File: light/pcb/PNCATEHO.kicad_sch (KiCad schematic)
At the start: 49 parts, among them J1 USB_C_Receptacle_USB2.0, U1 RP2040, U2 RT9013-33GB, U3 W25Q32JVSSIQ, Y1 12MHz

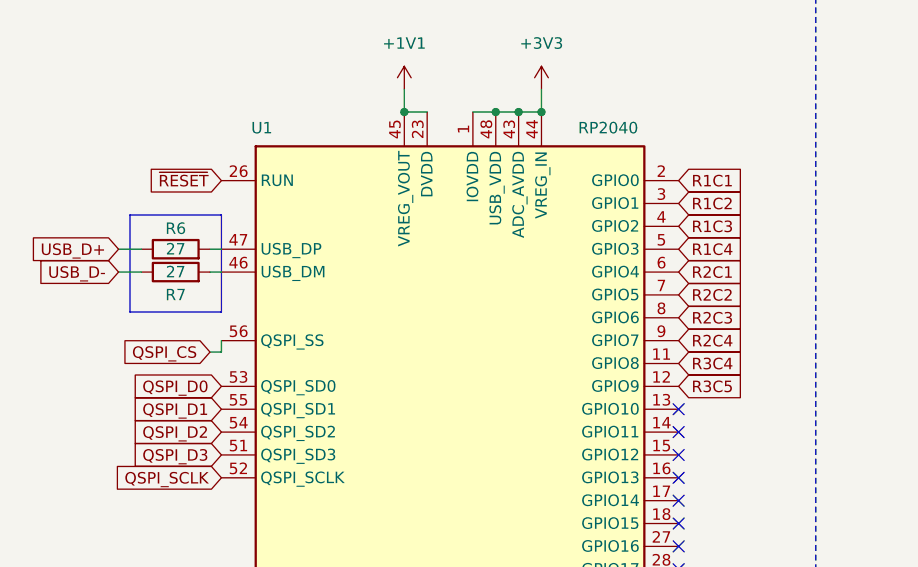
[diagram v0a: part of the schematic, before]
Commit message: PGS1316s PNCATEHO basic routing
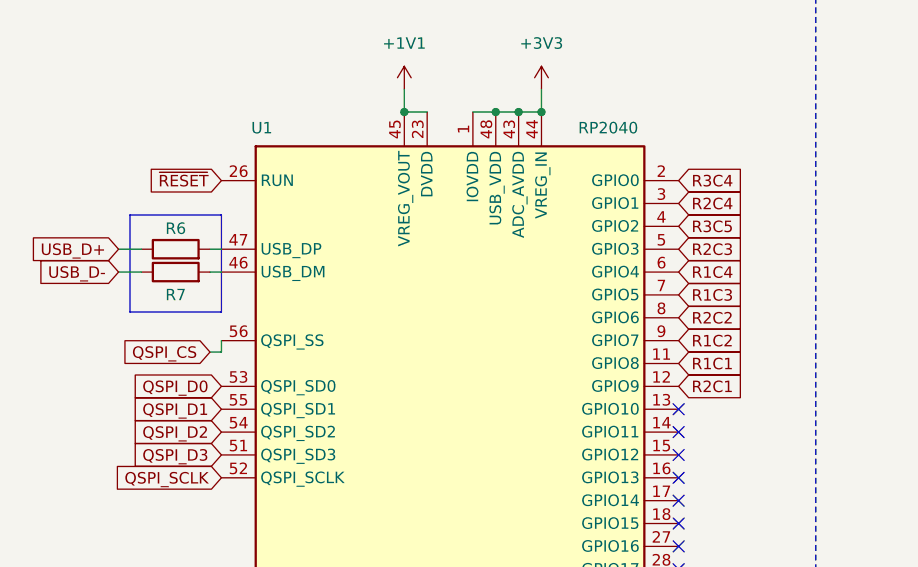
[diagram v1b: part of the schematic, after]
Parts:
- C1, C10, C11, C12, C13, C14, C15, C16, C2, C3, C4, C5, C6, C7, C8, C9: footprint footprint:C_0805_2012Metric_Pad1.18x1.45mm_HandSolder -> PNCATEHO:C_0805_2012Metric_Pad1.18x1.45mm_HandSolder
- D1, D2: footprint footprint:LED_0805_2012Metric_Pad1.15x1.40mm_HandSolder -> PNCATEHO:LED_0805_2012Metric_Pad1.15x1.40mm_HandSolder
- F1: footprint footprint:Fuse_0805_2012Metric -> PNCATEHO:Fuse_0805_2012Metric
- J1: footprint footprint:USB_C_Receptacle_TYPE-C-31-M-12 -> PNCATEHO:USB_C_Receptacle_TYPE-C-31-M-12
- R1, R10, R2, R3, R4, R5, R6, R7, R8, R9: footprint footprint:R_0805_2012Metric_Pad1.20x1.40mm_HandSolder -> PNCATEHO:R_0805_2012Metric_Pad1.20x1.40mm_HandSolder
- SW11, SW12: footprint footprint:SW_SMD_L4_W3_H1.5 -> PNCATEHO:SW_SMD_L4_W3_H1.5
- TP1, TP2, TP3: footprint footprint:TestPoint_Pad_D2.0mm -> PNCATEHO:TestPoint_Pad_D2.0mm
- U1: footprint footprint:RP2040-QFN-56 -> PNCATEHO:RP2040-QFN-56
- U2: footprint footprint:SOT-23-5_L3.0-W1.7-P0.95-LS2.8-BL -> PNCATEHO:SOT-23-5_L3.0-W1.7-P0.95-LS2.8-BL
- U3: footprint footprint:SOIC127P790X216-8N -> PNCATEHO:SOIC127P790X216-8N
- Y1: footprint footprint:Crystal_SMD_3225-4Pin_3.2x2.5mm -> PNCATEHO:Crystal_SMD_3225-4Pin_3.2x2.5mm
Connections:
- net R1C1: now also U1.11 (GPIO8); no longer U1.2 (GPIO0)
- net R1C2: now also U1.9 (GPIO7); no longer U1.3 (GPIO1)
- net R1C3: now also U1.7 (GPIO5); no longer U1.4 (GPIO2)
- net R1C4: now also U1.6 (GPIO4); no longer U1.5 (GPIO3)
- net R2C1: now also U1.12 (GPIO9); no longer U1.6 (GPIO4)
- net R2C2: now also U1.8 (GPIO6); no longer U1.7 (GPIO5)
- net R2C3: now also U1.5 (GPIO3); no longer U1.8 (GPIO6)
- net R2C4: now also U1.3 (GPIO1); no longer U1.9 (GPIO7)
- net R3C4: now also U1.2 (GPIO0); no longer U1.11 (GPIO8)
- net R3C5: now also U1.4 (GPIO2); no longer U1.12 (GPIO9)

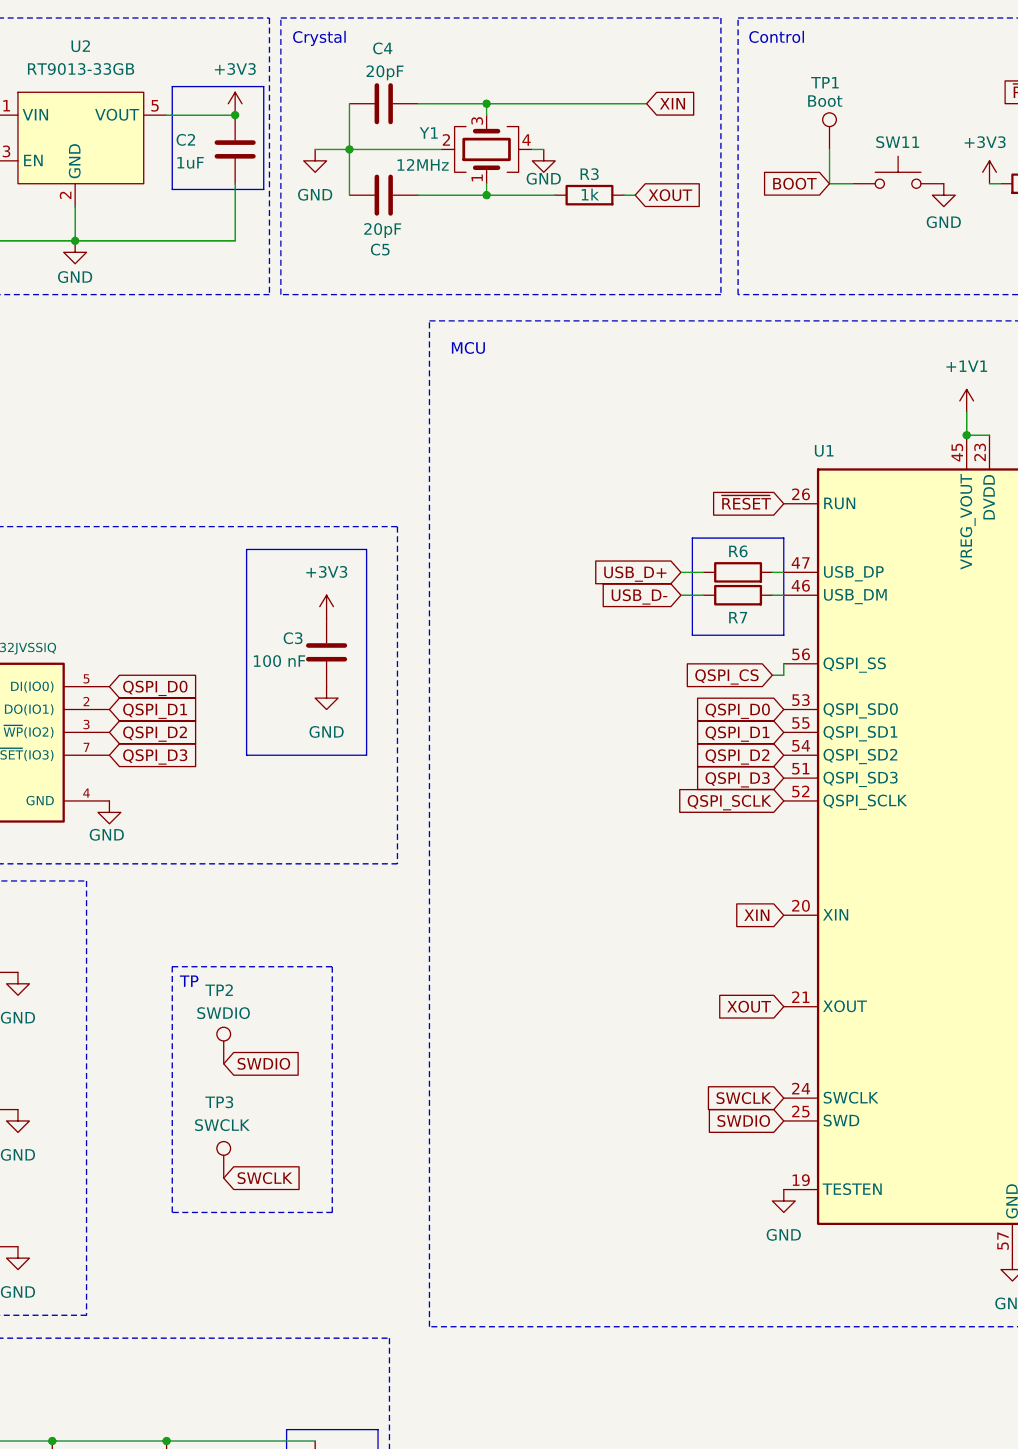
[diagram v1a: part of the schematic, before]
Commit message: update outline
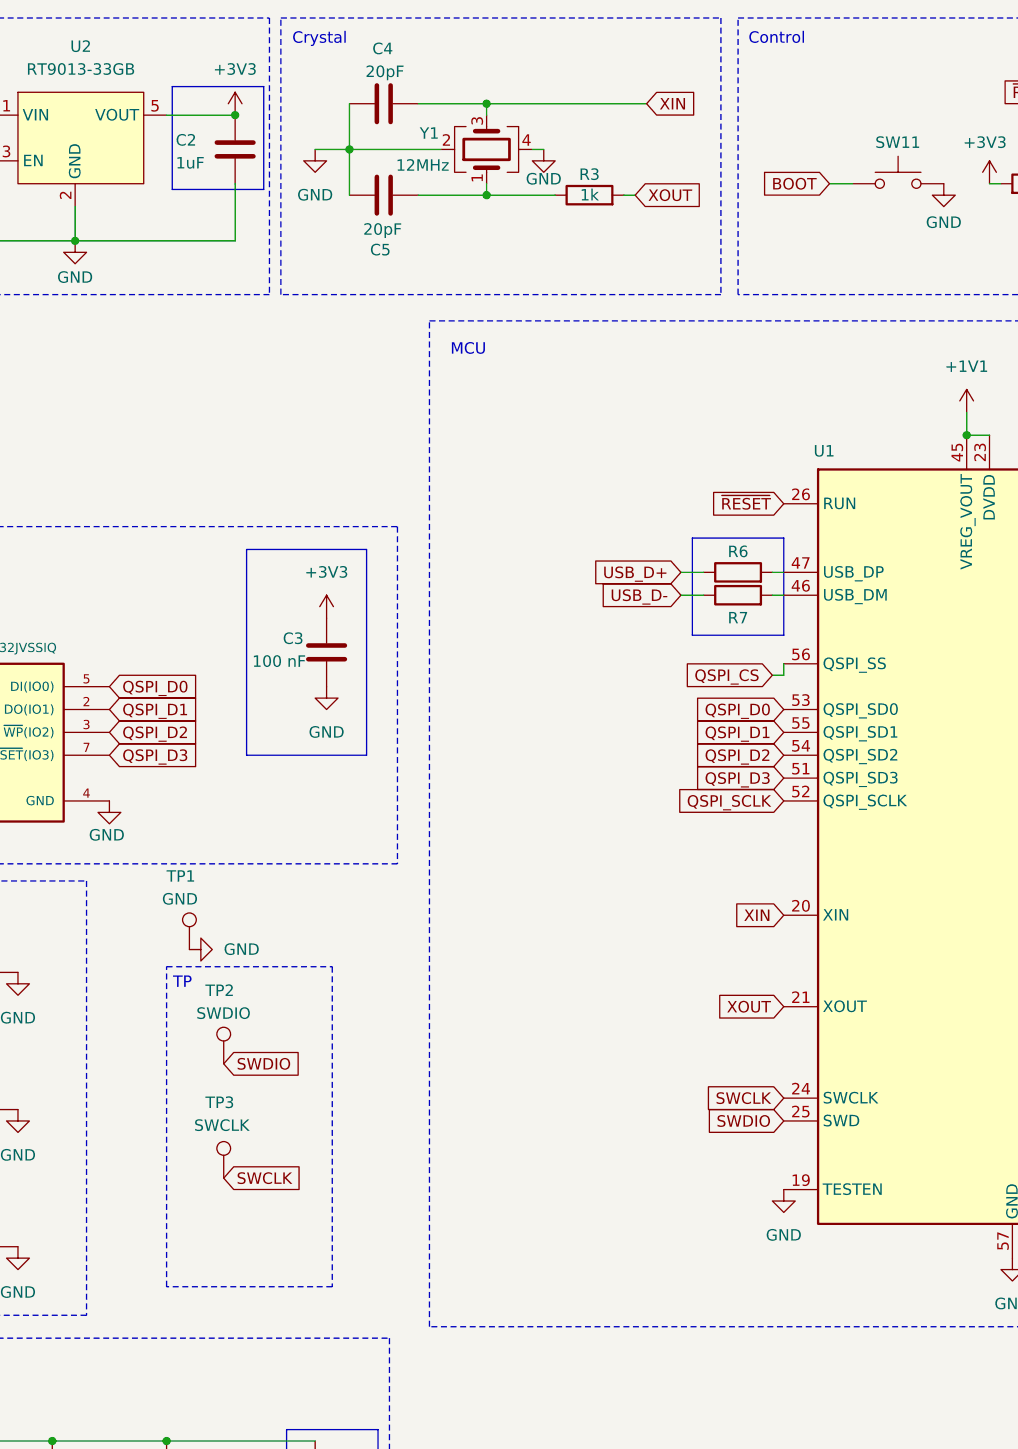
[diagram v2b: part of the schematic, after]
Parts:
- TP1: value Boot -> GND
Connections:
- net BOOT: no longer TP1.1
- net GND: now also TP1.1
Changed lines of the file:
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@@
 	)
 	(rectangle
-		(start 98.425 121.285)
-		(end 116.205 148.59)
+		(start 97.79 121.285)
+		(end 116.205 156.845)
 		(stroke
 			(width 0)
@@
 	(text "TP"
 		(exclude_from_sim no)
-		(at 100.33 123.19 0)
+		(at 99.568 123.19 0)
 		(effects
 			(font
@@
 	(wire
 		(pts
-			(xy 171.45 30.48) (xy 171.45 34.29)
-		)
-		(stroke
-			(width 0)
-			(type default)
-		)
-	)
-	(wire
-		(pts
 			(xy 58.42 31.75) (xy 55.88 31.75)
 		)
@@
 	(symbol
 		(lib_id "PNCATEHO:GND")
+		(at 100.33 119.38 90)
+		(unit 1)
+		(exclude_from_sim no)
+		(in_bom yes)
+		(on_board yes)
+		(dnp no)
+		(fields_autoplaced yes)
+		(property "Reference" "#PWR018"
+			(at 106.68 119.38 0)
+			(effects
+				(font
+					(size 1.27 1.27)
+				)
+				(hide yes)
+			)
+		)
+		(property "Value" "GND"
+			(at 104.14 119.3799 90)
+			(effects
+				(font
+					(size 1.27 1.27)
+				)
+				(justify right)
+			)
+		)
+		(property "Footprint" ""
+			(at 100.33 119.38 0)
+			(effects
+				(font
+					(size 1.27 1.27)
+				)
+				(hide yes)
+			)
+		)
+		(property "Datasheet" ""
+			(at 100.33 119.38 0)
+			(effects
+				(font
+					(size 1.27 1.27)
+				)
+				(hide yes)
+			)
+		)
+		(property "Description" "Global ground symbol"
+			(at 109.728 119.38 0)
+			(effects
+				(font
+					(size 1.27 1.27)
+				)
+				(hide yes)
+			)
+		)
+		(pin "1"
+		)
+		(instances
+			(project ""
+				(path "/02fc811b-599c-42c6-9c96-ff4b46846544"
+					(reference "#PWR018")
+					(unit 1)
+				)
+			)
+		)
+	)
+	(symbol
+		(lib_id "PNCATEHO:GND")
 		(at 214.63 34.29 0)
 		(mirror y)
@@
 	)
 	(symbol
-		(lib_id "PNCATEHO:TestPoint")
-		(at 171.45 30.48 0)
-		(unit 1)
-		(exclude_from_sim no)
-		(in_bom yes)
-		(on_board yes)
-		(dnp no)
-		(property "Reference" "TP1"
-			(at 169.418 23.114 0)
-			(effects
-				(font
-					(size 1.27 1.27)
-				)
-				(justify left)
-			)
-		)
-		(property "Value" "Boot"
-			(at 168.91 25.146 0)
-			(effects
-				(font
-					(size 1.27 1.27)
-				)
-				(justify left)
-			)
-		)
-		(property "Footprint" "PNCATEHO:TestPoint_Pad_D2.0mm"
-			(at 176.53 30.48 0)
-			(effects
-				(font
-					(size 1.27 1.27)
-				)
-				(hide yes)
-			)
-		)
-		(property "Datasheet" "~"
-			(at 176.53 30.48 0)
-			(effects
-				(font
-					(size 1.27 1.27)
-				)
-				(hide yes)
-			)
-		)
-		(property "Description" "test point"
-			(at 171.45 30.48 0)
-			(effects
-				(font
-					(size 1.27 1.27)
-				)
-				(hide yes)
-			)
-		)
-		(pin "1"
-		)
-		(instances
-			(project ""
-				(path "/02fc811b-599c-42c6-9c96-ff4b46846544"
-					(reference "TP1")
-					(unit 1)
-				)
-			)
-		)
-	)
-	(symbol
 		(lib_id "PNCATEHO:+3V3")
 		(at 68.58 82.55 0)
@@
 					(unit 1)
 				)
+			)
+		)
+	)
+	(symbol
+		(lib_id "PNCATEHO:TestPoint")
+		(at 100.33 119.38 0)
+		(unit 1)
+		(exclude_from_sim no)
+		(in_bom yes)
+		(on_board yes)
+		(dnp no)
+		(property "Reference" "TP1"
+			(at 97.79 111.252 0)
+			(effects
+				(font
+					(size 1.27 1.27)
+				)
+				(justify left)
+			)
+		)
+		(property "Value" "GND"
+			(at 97.282 113.7919 0)
+			(effects
+				(font
+					(size 1.27 1.27)
+				)
+				(justify left)
+			)
+		)
+		(property "Footprint" "PNCATEHO:TestPoint_Pad_D2.0mm"
+			(at 105.41 119.38 0)
+			(effects
+				(font
+					(size 1.27 1.27)
+				)
+				(hide yes)
+			)
+		)
+		(property "Datasheet" "~"
+			(at 105.41 119.38 0)
+			(effects
+				(font
+					(size 1.27 1.27)
+				)
+				(hide yes)
+			)
+		)
+		(property "Description" "test point"
+			(at 100.33 119.38 0)
+			(effects
+				(font
+					(size 1.27 1.27)
+				)
+				(hide yes)
+			)
+		)
+		(pin "1"
+		)
+		(instances
+			(project "PNCATEHO"
+				(path "/02fc811b-599c-42c6-9c96-ff4b46846544"
+					(reference "TP1")
+					(unit 1)
+				)

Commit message: Some little fixes
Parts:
- SW1, SW10, SW2, SW3, SW4, SW5, SW6, SW7, SW8, SW9: footprint switches:SW_PG1316 -> PNCATEHO:SW_PG1316
- SW11: value ~ -> Boot
- SW12: value ~ -> Reset
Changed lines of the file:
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@@
 			)
 		)
-		(property "Footprint" "switches:SW_PG1316"
+		(property "Footprint" "PNCATEHO:SW_PG1316"
 			(at 43.18 116.84 0)
 			(effects
@@
 			)
 		)
-		(property "Footprint" "switches:SW_PG1316"
+		(property "Footprint" "PNCATEHO:SW_PG1316"
 			(at 76.2 147.32 0)
 			(effects
@@
 			)
 		)
-		(property "Footprint" "switches:SW_PG1316"
+		(property "Footprint" "PNCATEHO:SW_PG1316"
 			(at 59.69 147.32 0)
 			(effects
@@
 			)
 		)
-		(property "Footprint" "switches:SW_PG1316"
+		(property "Footprint" "PNCATEHO:SW_PG1316"
 			(at 76.2 132.08 0)
 			(effects
@@
 			)
 		)
-		(property "Footprint" "switches:SW_PG1316"
+		(property "Footprint" "PNCATEHO:SW_PG1316"
 			(at 59.69 116.84 0)
 			(effects
@@
 			)
 		)
-		(property "Value" "~"
+		(property "Value" "Reset"
 			(at 209.55 35.814 0)
 			(effects
@@
 			)
 		)
-		(property "Footprint" "switches:SW_PG1316"
+		(property "Footprint" "PNCATEHO:SW_PG1316"
 			(at 59.69 132.08 0)
 			(effects
@@
 			)
 		)
-		(property "Value" "~"
+		(property "Value" "Boot"
 			(at 179.07 35.814 0)
 			(effects
@@
 			)
 		)
-		(property "Footprint" "switches:SW_PG1316"
+		(property "Footprint" "PNCATEHO:SW_PG1316"
 			(at 26.67 116.84 0)
 			(effects
@@
 			)
 		)
-		(property "Footprint" "switches:SW_PG1316"
+		(property "Footprint" "PNCATEHO:SW_PG1316"
 			(at 26.67 132.08 0)
 			(effects
@@
 			)
 		)
-		(property "Footprint" "switches:SW_PG1316"
+		(property "Footprint" "PNCATEHO:SW_PG1316"
 			(at 76.2 116.84 0)
 			(effects
@@
 			)
 		)
-		(property "Footprint" "switches:SW_PG1316"
+		(property "Footprint" "PNCATEHO:SW_PG1316"
 			(at 43.18 132.08 0)
 			(effects
